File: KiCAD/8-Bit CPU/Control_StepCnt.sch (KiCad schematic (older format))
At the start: 12 parts, among them U28 74HC00, U29 74HC161, U30 74HC32

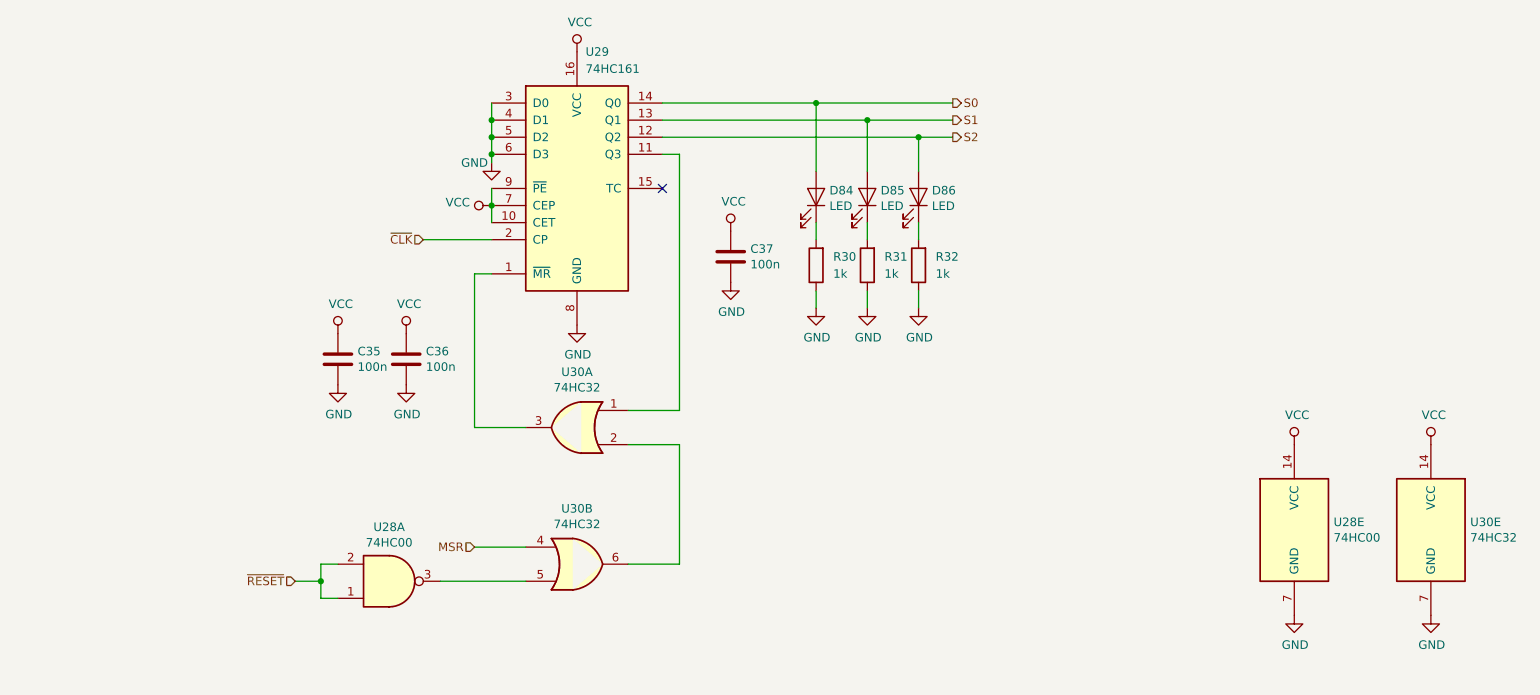
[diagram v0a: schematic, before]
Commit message: KiCAD cleanup - Revision A
Revision A Known Issues:
 * ATTiny45 has incorrect footprint
 * Flags register is redundant (The ATMega16's output port is a register)
 * Power jack pinout is wrong (12V shorted to ground)
 * Step counter reset logic is wrong (Active high signalling, Active low input)
 * ALU output indicator not connected
 * HLT indicator missing
 * EEPROMs can't be page written due to addressing setup (minor annoyance)
 * Flags Logic uses NAND gates instead of AND (fixed on the board I built)
 * Programmer needs to be able to toggle EEPROM outputs and Addressing Devices
    with different signals to enable reading.
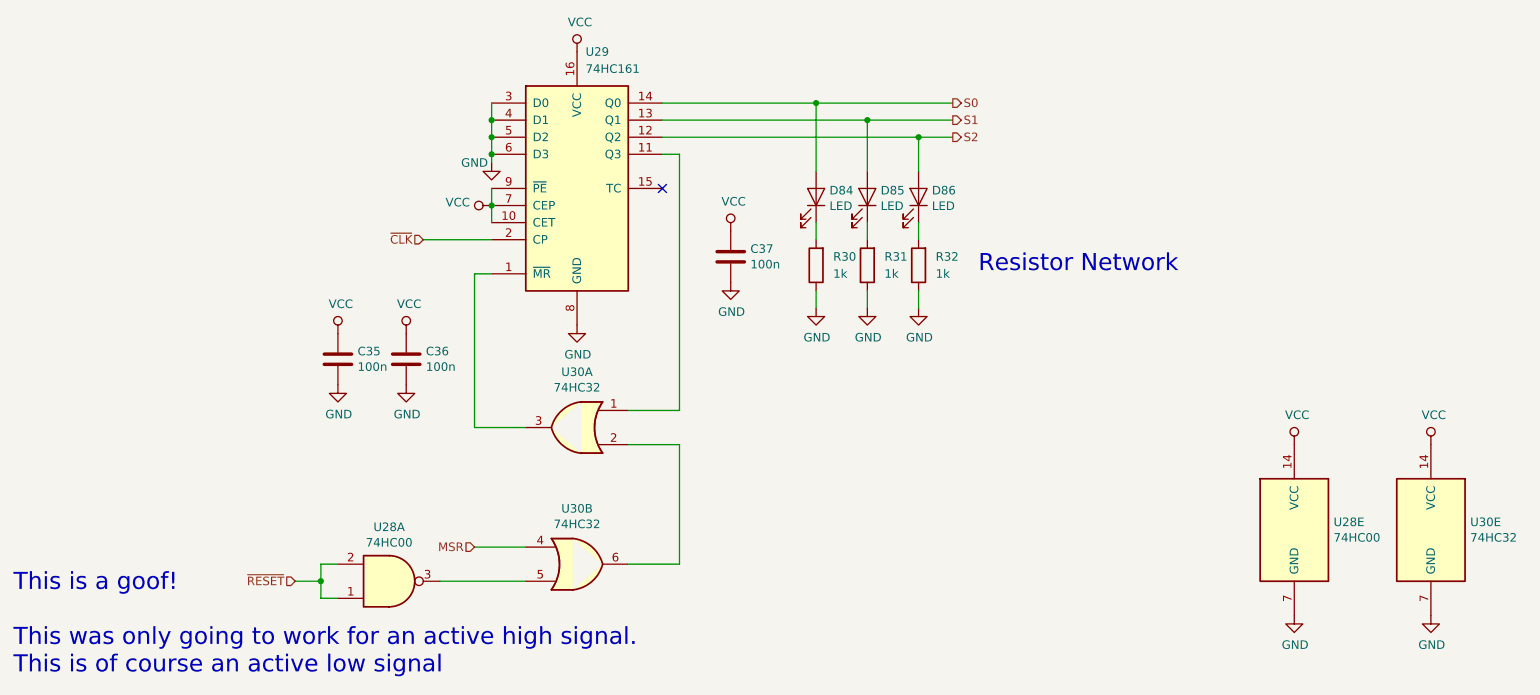
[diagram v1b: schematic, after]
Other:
- note added: "Resistor Network"
- note added: "This is a goof!\n\nThis was only going to work for an active high signal.\nThis is of course an active low signal"
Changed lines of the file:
@@
 $Descr A4 11693 8268
 encoding utf-8
-Sheet 19 30
+Sheet 19 29
 Title ""
 Date ""
@@
 Text HLabel 5000 5800 0    50   Input ~ 0
 MSR
+Text Notes 2300 6550 0    100  ~ 0
+This is a goof!\n\nThis was only going to work for an active high signal.\nThis is of course an active low signal
+Text Notes 7950 4200 0    100  ~ 0
+Resistor Network
 $EndSCHEMATC

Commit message: KiCAD files update & Gerbers
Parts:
- removed C35, C36: 100n, Capacitor_SMD:C_0805_2012Metric, symbol Device:C
- removed R30, R31, R32: 1k, Resistor_SMD:R_0805_2012Metric, symbol Device:R
- removed U28: 74HC00, jcf:SOIC-14_3.9x8.7mm_P1.27mm_JCF, symbol 74xx:74HC00
- removed U30: 74HC32, Package_SO:SOIC-14_3.9x8.7mm_P1.27mm, symbol 74xx:74LS32
- added RN30: 1k, Resistor_SMD:R_Array_Concave_4x0603, symbol Device:R_Pack04
- renumbered D84 to D88, D85 to D89, D86 to D90, U29 to U30
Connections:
- net GND: now also RN30.5 (R4.2), RN30.6 (R3.2), RN30.7 (R2.2)
- net VCC: no longer U30.9 (~PE)
- net ~RESET: now also U30.1 (~MR)
- net at D88.1 (K): now also RN30.4 (R4.1)
- net at D89.1 (K): now also RN30.3 (R3.1)
- net at D90.1 (K): now also RN30.2 (R2.1)
- new net ~MSR: U30.9 (~PE)
- no-connect marks 1 -> 4
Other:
- note removed: "Resistor Network"
- note removed: "This is a goof!\n\nThis was only going to work for an active high signal.\nThis is of course an active low signal"
